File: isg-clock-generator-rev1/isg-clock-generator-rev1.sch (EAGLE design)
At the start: 160 parts, among them IC1 LMK03318RHSR, IC4 TPS7A8001DRBR, IC5 TPS7A8001DRBR, Q1 7M50072001, X1 OUT2_P, X2 OUT2_N, X3 OUT0_P, X4 PRIREF_P, X5 PRIREF_N, X6 V_IN_EXT

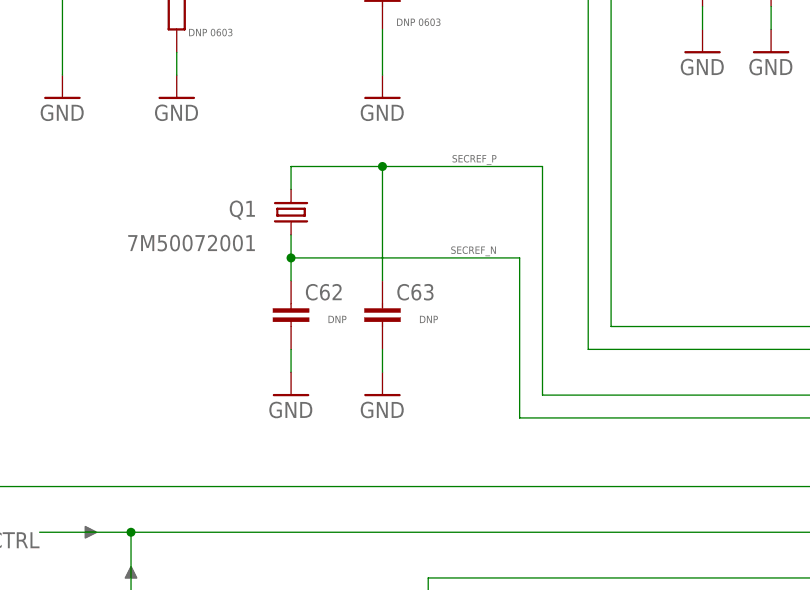
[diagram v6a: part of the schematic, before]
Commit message: Crystal package fixed and routed
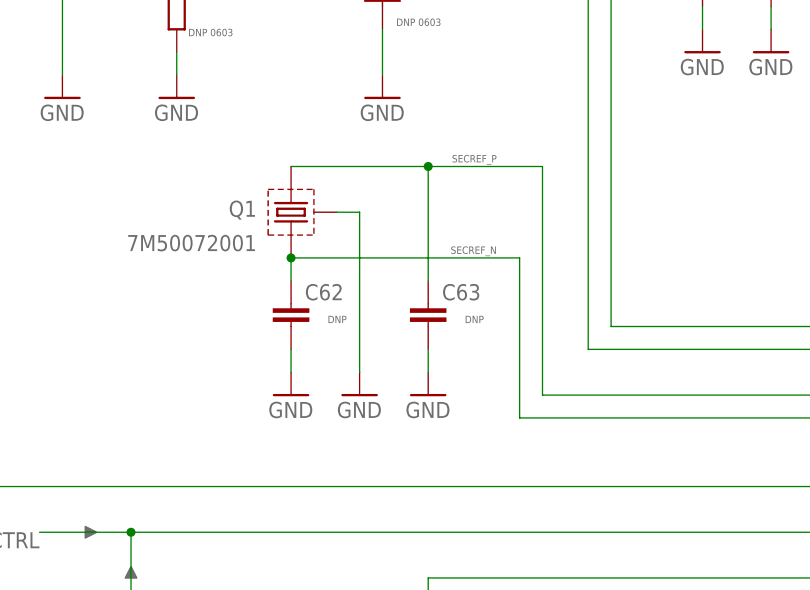
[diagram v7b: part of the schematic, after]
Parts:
- Q1: device crystal-geyer_V1_0:KX-7 -> isg-clock-generator:KX-7
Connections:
- net GND: now also Q1.GND
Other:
- moved on the sheet: C63
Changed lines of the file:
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@@
 <part name="X2" library="con-coax" library_urn="urn:adsk.eagle:library:133" deviceset="SMA-" device="142-0701-881/886" package3d_urn="urn:adsk.eagle:package:6216/1" value="OUT2_N"/>
 <part name="X3" library="con-coax" library_urn="urn:adsk.eagle:library:133" deviceset="SMA-" device="142-0701-881/886" package3d_urn="urn:adsk.eagle:package:6216/1" value="OUT0_P"/>
-<part name="Q1" library="crystal-geyer_V1_0" library_urn="urn:adsk.eagle:library:203" deviceset="KX" device="-7" package3d_urn="urn:adsk.eagle:package:11924/1" value="7M50072001"/>
+<part name="Q1" library="isg-clock-generator" deviceset="KX" device="-7" package3d_urn="urn:adsk.eagle:package:11924/1" value="7M50072001"/>
 <part name="C1" library="rcl-modified-footprints" deviceset="C-EU" device="C0603" package3d_urn="urn:adsk.eagle:package:23616/2" value="CAP CER 10uF 6.3V X5R 0603"/>
 <part name="C2" library="rcl-modified-footprints" deviceset="C-EU" device="C0603" package3d_urn="urn:adsk.eagle:package:23616/2" value="CAP CER 10uF 6.3V X5R 0603"/>
@@
 <part name="GND90" library="supply1" library_urn="urn:adsk.eagle:library:371" deviceset="GND" device=""/>
 <part name="GND91" library="supply1" library_urn="urn:adsk.eagle:library:371" deviceset="GND" device=""/>
+<part name="GND92" library="supply1" library_urn="urn:adsk.eagle:library:371" deviceset="GND" device=""/>
 </parts>
 <sheets>
@@
 <attribute name="VALUE" x="105.664" y="168.021" size="0.8128" layer="96"/>
 </instance>
-<instance part="C63" gate="G$1" x="111.76" y="170.18" smashed="yes">
-<attribute name="NAME" x="113.284" y="170.561" size="1.778" layer="95"/>
-<attribute name="VALUE" x="115.824" y="168.021" size="0.8128" layer="96"/>
+<instance part="C63" gate="G$1" x="116.84" y="170.18" smashed="yes">
+<attribute name="NAME" x="118.364" y="170.561" size="1.778" layer="95"/>
+<attribute name="VALUE" x="120.904" y="168.021" size="0.8128" layer="96"/>
 </instance>
-<instance part="GND84" gate="1" x="111.76" y="160.02" smashed="yes">
-<attribute name="VALUE" x="109.22" y="157.48" size="1.778" layer="96"/>
+<instance part="GND84" gate="1" x="116.84" y="160.02" smashed="yes">
+<attribute name="VALUE" x="114.3" y="157.48" size="1.778" layer="96"/>
 </instance>
 <instance part="GND85" gate="1" x="101.6" y="160.02" smashed="yes">
@@
 <attribute name="VALUE" x="520.7" y="185.42" size="1.778" layer="96"/>
 </instance>
+<instance part="GND92" gate="1" x="109.22" y="160.02" smashed="yes">
+<attribute name="VALUE" x="106.68" y="157.48" size="1.778" layer="96"/>
+</instance>
 </instances>
 <busses>
@@
 <pinref part="GND84" gate="1" pin="GND"/>
 <pinref part="C63" gate="G$1" pin="2"/>
-<wire x1="111.76" y1="162.56" x2="111.76" y2="165.1" width="0.1524" layer="91"/>
+<wire x1="116.84" y1="162.56" x2="116.84" y2="165.1" width="0.1524" layer="91"/>
 </segment>
 <segment>
@@
 <wire x1="523.24" y1="190.5" x2="523.24" y2="193.04" width="0.1524" layer="91"/>
 </segment>
+<segment>
+<pinref part="GND92" gate="1" pin="GND"/>
+<wire x1="109.22" y1="162.56" x2="109.22" y2="180.34" width="0.1524" layer="91"/>
+<pinref part="Q1" gate="G$1" pin="GND"/>
+<wire x1="109.22" y1="180.34" x2="106.68" y2="180.34" width="0.1524" layer="91"/>
+</segment>
 </net>
 <net name="DECAP_LDO" class="0">
@@
 <wire x1="314.96" y1="160.02" x2="129.54" y2="160.02" width="0.1524" layer="91"/>
 <pinref part="Q1" gate="G$1" pin="2"/>
-<wire x1="101.6" y1="182.88" x2="101.6" y2="185.42" width="0.1524" layer="91"/>
-<wire x1="101.6" y1="185.42" x2="111.76" y2="185.42" width="0.1524" layer="91"/>
+<wire x1="101.6" y1="185.42" x2="116.84" y2="185.42" width="0.1524" layer="91"/>
 <pinref part="C63" gate="G$1" pin="1"/>
-<wire x1="111.76" y1="185.42" x2="111.76" y2="172.72" width="0.1524" layer="91"/>
+<wire x1="116.84" y1="185.42" x2="116.84" y2="172.72" width="0.1524" layer="91"/>
 <wire x1="129.54" y1="160.02" x2="129.54" y2="185.42" width="0.1524" layer="91"/>
-<wire x1="129.54" y1="185.42" x2="111.76" y2="185.42" width="0.1524" layer="91"/>
-<junction x="111.76" y="185.42"/>
+<wire x1="129.54" y1="185.42" x2="116.84" y2="185.42" width="0.1524" layer="91"/>
+<junction x="116.84" y="185.42"/>
 <label x="312.42" y="161.29" size="0.8128" layer="95" rot="R180"/>
 <label x="124.46" y="186.69" size="0.8128" layer="95" rot="R180"/>
@@
 <pinref part="Q1" gate="G$1" pin="1"/>
 <wire x1="101.6" y1="172.72" x2="101.6" y2="175.26" width="0.1524" layer="91"/>
-<wire x1="101.6" y1="175.26" x2="101.6" y2="177.8" width="0.1524" layer="91"/>
 <wire x1="101.6" y1="175.26" x2="127" y2="175.26" width="0.1524" layer="91"/>
 <junction x="101.6" y="175.26"/>

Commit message: More routing, decaps and config headers
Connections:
- net N$24 renamed GPIO4_JUMPER
- net N$25 renamed GPIO3_JUMPER
- net N$26 renamed GPIO0_JUMPER
- net N$27 renamed GPIO2_JUMPER
- net N$28 renamed HWCTRL_JUMPER
- net N$29 renamed GPIO1_JUMPER
- net N$31 renamed REFSEL_JUMPER
- net N$4 renamed PULLUP_GPIO5
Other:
- note added: "XTAL: SecRef only"
- note removed: "XTAL: SecRef only Todo: get symbol with grounded pads"
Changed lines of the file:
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@@
 Can unused VDDO pins be left unpowered?</text>
 <text x="302.26" y="93.98" size="1.778" layer="98">HWCTRL state is sampled on POR and determines the mode of operation.</text>
-<text x="71.12" y="180.34" size="1.778" layer="98">XTAL: SecRef only
-Todo: get symbol
-with grounded pads</text>
+<text x="99.06" y="185.42" size="1.778" layer="98" rot="R180">XTAL: SecRef only</text>
 <text x="449.58" y="101.6" size="1.778" layer="98">LDOs step-down the output driver supply to 1.8 V internally.
 "VDDO4...7 can be GND if the output dividers are disabled"</text>
@@
 </segment>
 </net>
-<net name="N$4" class="0">
+<net name="PULLUP_GPIO5" class="0">
 <segment>
 <pinref part="JP3" gate="1" pin="3"/>
@@
 <pinref part="R16" gate="G$1" pin="1"/>
 <wire x1="266.7" y1="91.44" x2="266.7" y2="101.6" width="0.1524" layer="91"/>
+<label x="265.43" y="101.6" size="0.8128" layer="95" rot="R270"/>
 </segment>
 </net>
@@
 </segment>
 </net>
-<net name="N$24" class="0">
+<net name="GPIO4_JUMPER" class="0">
 <segment>
 <pinref part="JP4" gate="1" pin="2"/>
@@
 <pinref part="R27" gate="G$1" pin="1"/>
 <wire x1="241.3" y1="88.9" x2="241.3" y2="91.44" width="0.1524" layer="91"/>
-</segment>
-</net>
-<net name="N$25" class="0">
+<label x="231.14" y="87.63" size="0.8128" layer="95"/>
+</segment>
+</net>
+<net name="GPIO3_JUMPER" class="0">
 <segment>
 <pinref part="JP5" gate="1" pin="2"/>
@@
 <pinref part="R30" gate="G$1" pin="1"/>
 <wire x1="208.28" y1="88.9" x2="208.28" y2="91.44" width="0.1524" layer="91"/>
+<label x="198.12" y="87.63" size="0.8128" layer="95"/>
 </segment>
 </net>
@@
 </segment>
 </net>
-<net name="N$27" class="0">
+<net name="GPIO2_JUMPER" class="0">
 <segment>
 <pinref part="JP6" gate="1" pin="2"/>
@@
 <pinref part="R33" gate="G$1" pin="1"/>
 <wire x1="175.26" y1="88.9" x2="175.26" y2="91.44" width="0.1524" layer="91"/>
+<label x="165.1" y="87.63" size="0.8128" layer="95"/>
 </segment>
 </net>
@@
 </segment>
 </net>
-<net name="N$29" class="0">
+<net name="GPIO1_JUMPER" class="0">
 <segment>
 <pinref part="JP7" gate="1" pin="2"/>
@@
 <pinref part="R36" gate="G$1" pin="1"/>
 <wire x1="142.24" y1="88.9" x2="142.24" y2="91.44" width="0.1524" layer="91"/>
+<label x="132.08" y="87.63" size="0.8128" layer="95"/>
 </segment>
 </net>
@@
 </segment>
 </net>
-<net name="N$26" class="0">
+<net name="GPIO0_JUMPER" class="0">
 <segment>
 <pinref part="JP8" gate="1" pin="2"/>
@@
 <pinref part="R39" gate="G$1" pin="1"/>
 <wire x1="116.84" y1="88.9" x2="116.84" y2="91.44" width="0.1524" layer="91"/>
+<label x="106.68" y="87.63" size="0.8128" layer="95"/>
 </segment>
 </net>
@@
 </segment>
 </net>
-<net name="N$28" class="0">
+<net name="HWCTRL_JUMPER" class="0">
 <segment>
 <pinref part="JP9" gate="1" pin="2"/>
@@
 <pinref part="R40" gate="G$1" pin="1"/>
 <wire x1="83.82" y1="88.9" x2="83.82" y2="91.44" width="0.1524" layer="91"/>
-</segment>
-</net>
-<net name="N$31" class="0">
+<label x="73.66" y="87.63" size="0.8128" layer="95"/>
+</segment>
+</net>
+<net name="REFSEL_JUMPER" class="0">
 <segment>
 <pinref part="JP10" gate="1" pin="2"/>
@@
 <pinref part="R43" gate="G$1" pin="1"/>
 <wire x1="50.8" y1="88.9" x2="50.8" y2="91.44" width="0.1524" layer="91"/>
-</segment>
-</net>
+<label x="40.64" y="87.63" size="0.8128" layer="95"/>
+</segment>
+</net>
